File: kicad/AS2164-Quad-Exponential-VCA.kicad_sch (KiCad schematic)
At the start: 71 parts, among them J1 CV1, J10 CV4, J11 Audio_in_4, J12 Audio_out_4, J2 Audio_in_1, J3 Audio_out_1, J4 CV2, J5 Audio_in_2, J6 Audio_out_2, J7 CV3, J8 Audio_in_3, J9 Audio_out_3, U1 TL074, U2 AS2164, U3 TL074

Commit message: added Schematic Revision 0.1.1
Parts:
- R11, R18, R25, R4: value 30K -> 100K
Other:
- note added: "VCA Inputs Vc1, Vc2, Vc3, Vc4 3.3V = 100% attenuation 0V = unity gain Vc < 0V = +20dB gain"
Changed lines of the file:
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@@
     (title "Eurorack AS2164 Quad Exponential VCA")
     (date "2024-01-25")
-    (rev "0.1.0")
+    (rev "0.1.1")
     (company "DIYSynthMNL")
     (comment 1 "This version is a prototype")
@@
     (effects (font (size 3 3)) (justify left bottom))
   )
+  (text "10Vpp" (at 270.51 45.72 0)
+    (effects (font (size 1.27 1.27)) (justify left bottom))
+  )
   (text "10Vpp" (at 177.8 115.57 0)
     (effects (font (size 1.27 1.27)) (justify left bottom))
@@
     (effects (font (size 2 2)) (justify left bottom))
   )
+  (text "10Vpp" (at 124.46 106.68 0)
+    (effects (font (size 1.27 1.27)) (justify left bottom))
+  )
   (text "0-5V" (at 13.97 91.44 0)
     (effects (font (size 1.27 1.27)) (justify left bottom))
@@
     (effects (font (size 1.27 1.27)) (justify left bottom))
   )
+  (text "10Vpp" (at 270.51 106.68 0)
+    (effects (font (size 1.27 1.27)) (justify left bottom))
+  )
   (text "0-5V" (at 158.75 30.48 0)
     (effects (font (size 1.27 1.27)) (justify left bottom))
@@
     (effects (font (size 2 2)) (justify left bottom))
   )
+  (text "10Vpp" (at 125.73 45.72 0)
+    (effects (font (size 1.27 1.27)) (justify left bottom))
+  )
   (text "0-5V" (at 158.75 91.44 0)
     (effects (font (size 1.27 1.27)) (justify left bottom))
@@
     (effects (font (size 2 2)) (justify left bottom))
   )
+  (text "VCA Inputs Vc1, Vc2, Vc3, Vc4\n3.3V = 100% attenuation\n0V = unity gain\nVc < 0V = +20dB gain"
+    (at 83.82 24.13 0)
+    (effects (font (size 1.27 1.27)) (justify left bottom))
+  )
   (text "10Vpp" (at 177.8 54.61 0)
     (effects (font (size 1.27 1.27)) (justify left bottom))
@@
       (effects (font (size 1.27 1.27)))
     )
-    (property "Value" "30K" (at 102.87 107.95 90)
+    (property "Value" "100K" (at 102.87 107.95 90)
       (effects (font (size 1.27 1.27)))
     )
@@
       (effects (font (size 1.27 1.27)))
     )
-    (property "Value" "30K" (at 247.65 46.99 90)
+    (property "Value" "100K" (at 247.65 46.99 90)
       (effects (font (size 1.27 1.27)))
     )
@@
       (effects (font (size 1.27 1.27)))
     )
-    (property "Value" "30K" (at 247.65 107.95 90)
+    (property "Value" "100K" (at 247.65 107.95 90)
       (effects (font (size 1.27 1.27)))
     )
@@
       (effects (font (size 1.27 1.27)))
     )
-    (property "Value" "30K" (at 102.87 46.99 90)
+    (property "Value" "100K" (at 102.87 46.99 90)
       (effects (font (size 1.27 1.27)))
     )

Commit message: schematic rev 0.1.1 notes added
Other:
- note added: "Module CV inputs (jacks) 0V CV = 100% attenuation 5V CV = Unity Gain"
- note removed: "0V CV = 100% attenuation 5V CV = Unity Gain"
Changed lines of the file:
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@@
     (effects (font (size 1.27 1.27)) (justify left bottom))
   )
-  (text "0V CV = 100% attenuation\n5V CV = Unity Gain" (at 180.34 143.51 0)
+  (text "Module CV inputs (jacks)\n0V CV = 100% attenuation\n5V CV = Unity Gain"
+    (at 180.34 148.59 0)
     (effects (font (size 1.27 1.27)) (justify left bottom))
   )
@@
   )
   (text "VCA Inputs Vc1, Vc2, Vc3, Vc4\n3.3V = 100% attenuation\n0V = unity gain\nVc < 0V = +20dB gain"
-    (at 83.82 24.13 0)
+    (at 180.34 158.75 0)
     (effects (font (size 1.27 1.27)) (justify left bottom))
   )

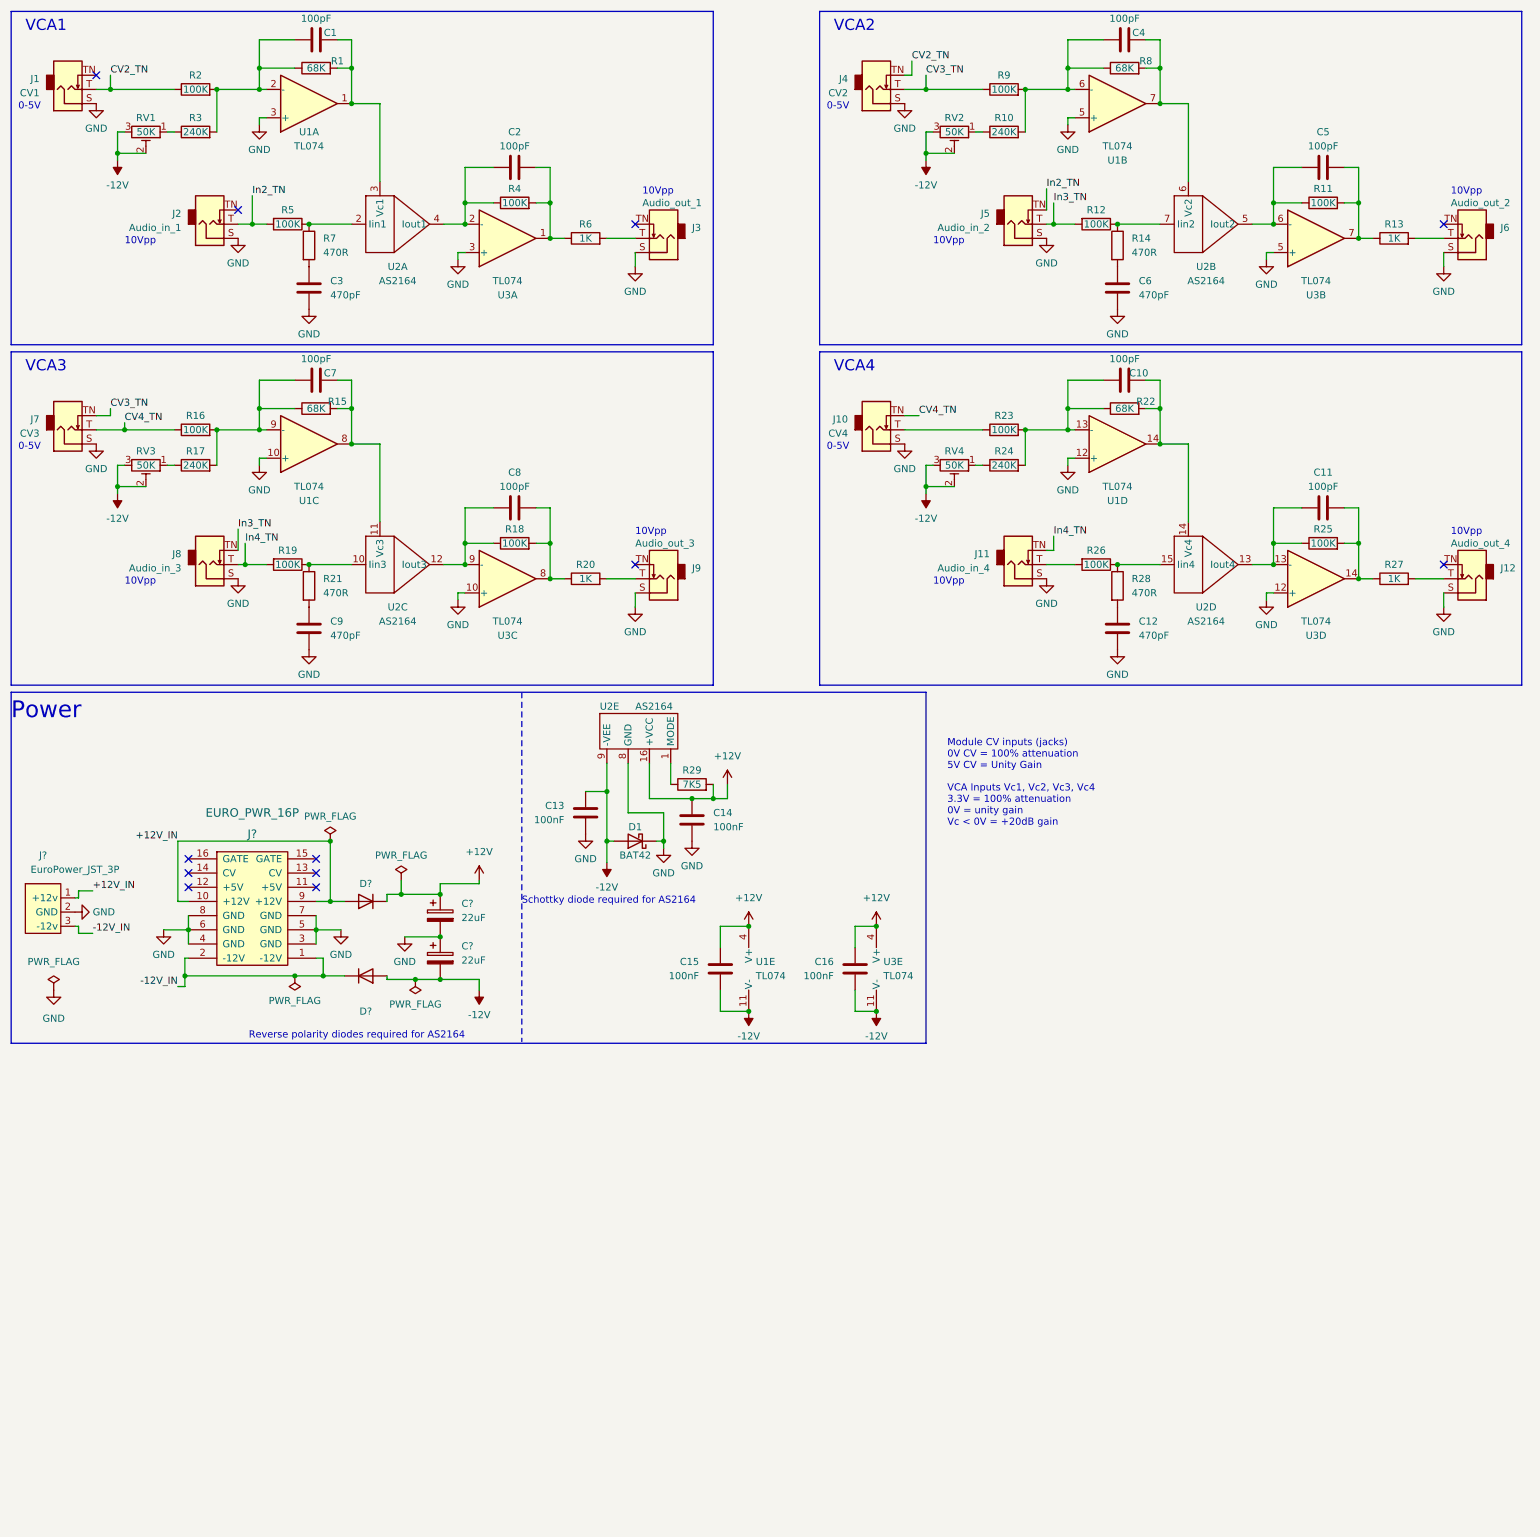
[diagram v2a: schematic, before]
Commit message: Added schematic rev 0.1.2
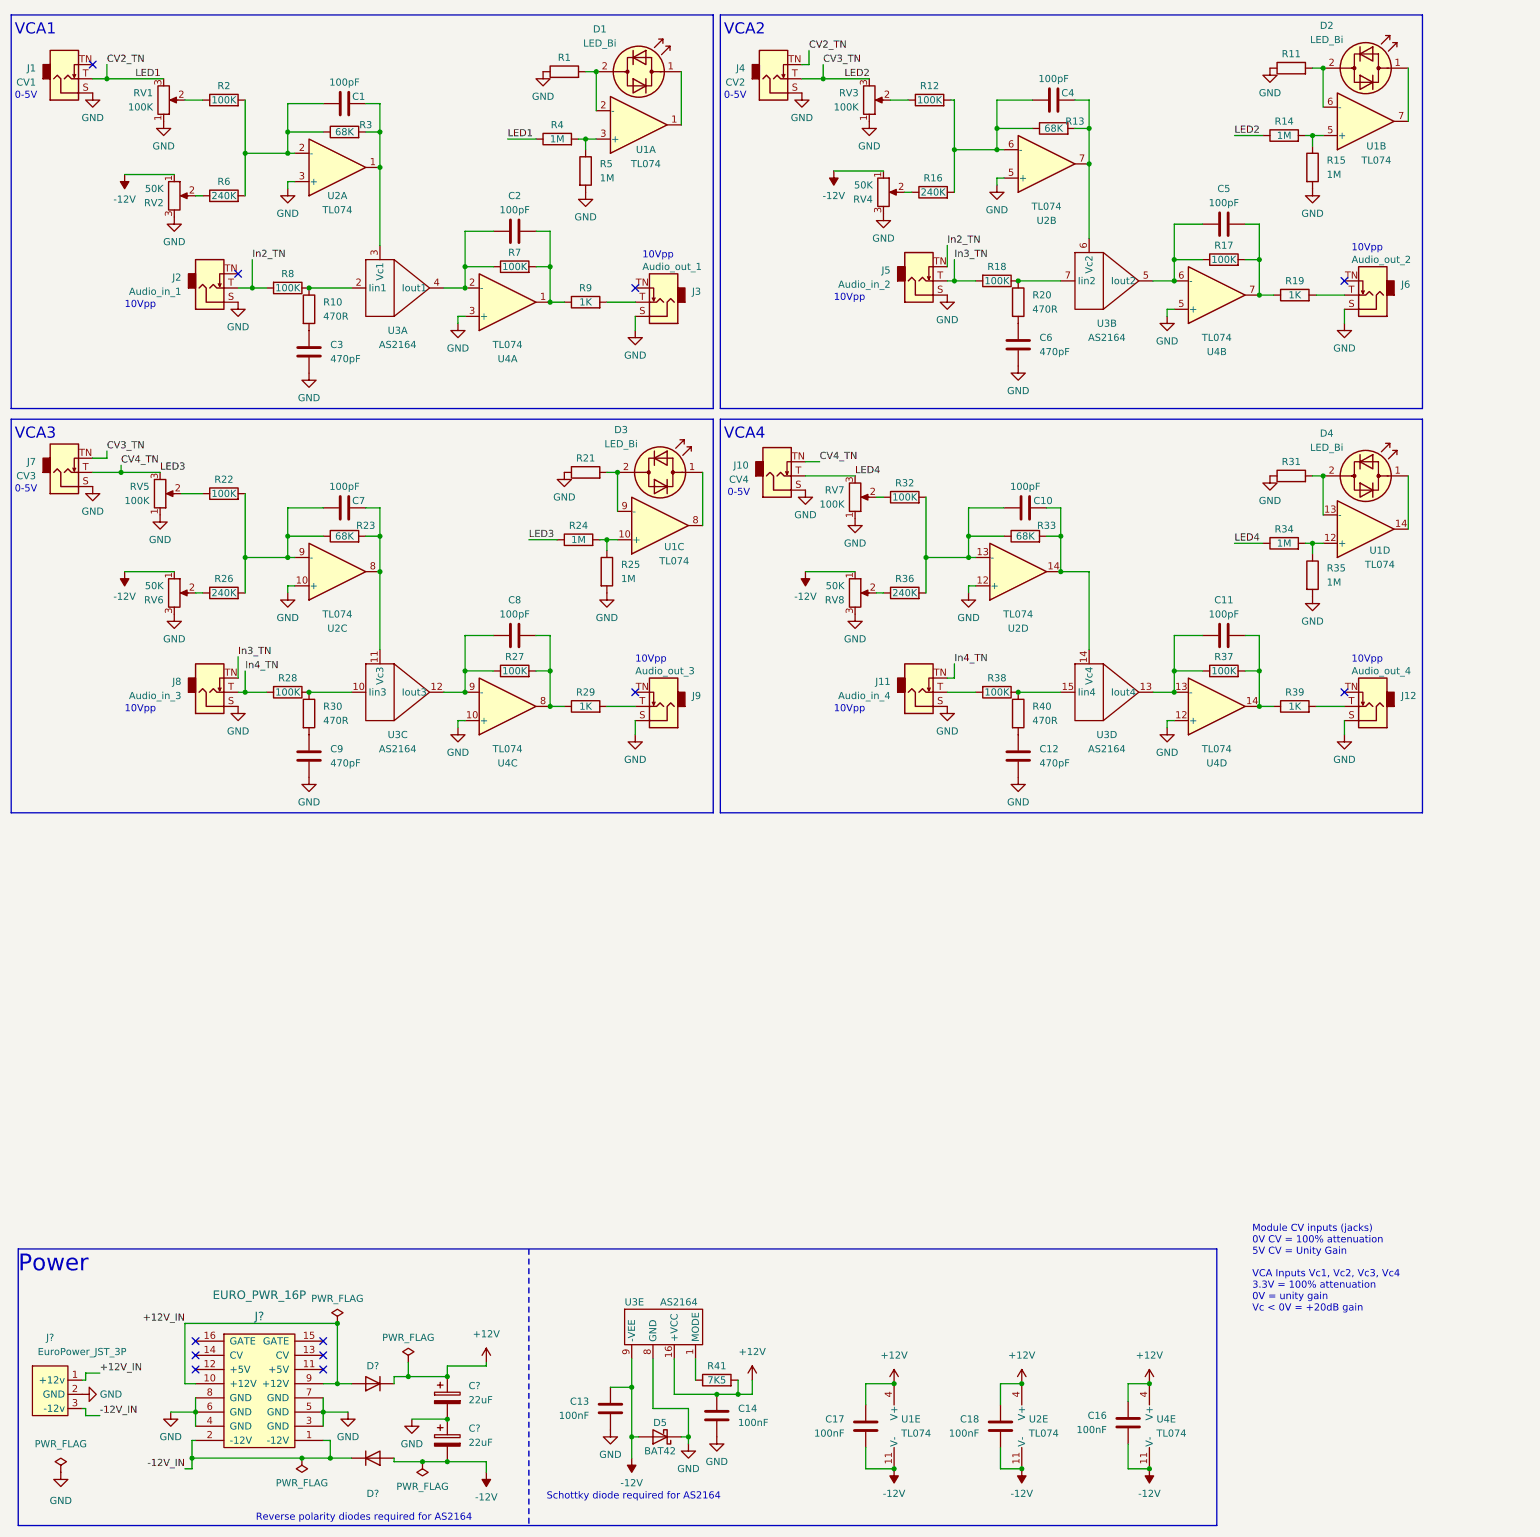
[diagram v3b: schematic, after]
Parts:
- removed RV1, RV2, RV3, RV4: 50K, symbol Device:R_Potentiometer_Trim
- added C16: 100nF, symbol Device:C
- added D1, D2, D3, D4: LED_Bi, symbol Device:LED_Dual_Bidirectional
- added R1, R11, R21, R31: ~, symbol Device:R
- added R14, R15, R24, R25, R34, R35, R4, R5: 1M, symbol Device:R
- added RV1, RV3, RV5, RV7: 100K, symbol Device:R_Potentiometer
- added RV2, RV4, RV6, RV8: 50K, symbol Device:R_Potentiometer
- added unit 4 of U1
- added unit 3 of U1
- added unit 2 of U1
- added unit 1 of U1
- added unit 5 of U4
- renumbered C15 to C17, C16 to C18, D1 to D5, R7 to R10, R9 to R12, R8 to R13, R10 to R16, R11 to R17, R12 to R18, R13 to R19, R14 to R20, R16 to R22, R15 to R23, R17 to R26, R18 to R27, R19 to R28, R20 to R29, R1 to R3, R21 to R30, R23 to R32, R22 to R33, R24 to R36, R25 to R37, R26 to R38, R27 to R39, R28 to R40, R29 to R41, R3 to R6, R4 to R7, R5 to R8, R6 to R9, U1 to U2, U3 to U2, U2 to U3, U3 to U4
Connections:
- net +12V: now also C16.1, U4.4 (V+)
- net -12V: now also C16.2, RV2.1, RV4.1, RV6.1, RV8.1, U4.11 (V-)
- net CV2_TN: now also R4.1, RV1.3; no longer R2.1
- net CV3_TN: now also R14.1, RV3.3; no longer R12.1
- net CV4_TN: now also R24.1, RV5.3; no longer R22.1
- net GND: now also R1.1, R11.1, R15.2, R21.1, R25.2, R31.1, R35.2, R5.2, RV1.1, RV2.3, RV3.1, RV4.3, RV5.1, RV6.3, RV7.1, RV8.3
- net at R36.1: now also RV8.2
- net at R16.1: now also RV4.2
- net at R32.1: now also RV7.2; no longer J10.T
- net at R26.1: now also RV6.2
- net at R6.1: now also RV2.2
- new net: R34.2, R35.1, U1.12 (+)
- new net: D4.2 (AK), R31.2, U1.13 (-)
- new net: D4.1 (KA), U1.14
- new net: R24.2, R25.1, U1.10 (+)
- new net: D3.1 (KA), U1.8
- new net: D3.2 (AK), R21.2, U1.9 (-)
- new net: R14.2, R15.1, U1.5 (+)
- new net: R12.1, RV3.2
- new net: D2.1 (KA), U1.7
- new net: D2.2 (AK), R11.2, U1.6 (-)
- new net: D1.1 (KA), U1.1
- new net: D1.2 (AK), R1.2, U1.2 (-)
- new net: R2.1, RV1.2
- new net: R4.2, R5.1, U1.3 (+)
- new net: R22.1, RV5.2
- new net LED4: J10.T, R34.1, RV7.3
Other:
- moved on the sheet: C1, C10, C11, C12, C13, C14, C17, C18, C2, C3, C4, C5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

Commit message: added schem rev0.1.3
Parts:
- added C20: 100nF, symbol Device:C
- added C21, C22: 100pF, symbol Device:C
- added JP1: Mix/VCA4, symbol Jumper:Jumper_3_Bridged12
- added R42, R43, R44, R45, R46, R47, R48: 100K, symbol Device:R
- added U5: TL072, symbol Amplifier_Operational:TL072
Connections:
- net +12V: now also C20.1, U5.8 (V+)
- net -12V: now also C20.2, U5.4 (V-)
- net GND: now also U5.3 (+), U5.5 (+)
- net O1: now reaches C2.2, R7.2, R9.1, U4.1
- net O1: now also R43.1
- net O2: now reaches C5.2, R17.2, R19.1, U4.7
- net O2: now also R44.1
- net O3: now reaches C8.2, R27.2, R29.1, U4.8
- net O3: now also R45.1
- net O4: now reaches C11.2, R37.2, U4.14
- net O4: now also JP1.3 (B), R46.1; no longer R39.1
- new net: C22.1, R47.2, R48.1, U5.6 (-)
- new net: C21.2, R42.2, R47.1, U5.1
- new net: C21.1, R42.1, R43.2, R44.2, R45.2, R46.2, U5.2 (-)
- new net: JP1.2 (C), R39.1
- new net Mix Out: C22.2, JP1.1 (A), R48.2, U5.7
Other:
- note added: "Audio Out 4 select"
- note added: "Mix"
- moved on the sheet: J12, R39

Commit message: Add revision 0.1.4
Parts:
- added D10, D11, D12, D13, D14, D15, D8, D9: BAT42, symbol Device:D_Schottky
- R47, R48: value 100K -> 10K
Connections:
- net at U2.7, U3.6 (Vc2): now also D10.2 (A), D11.1 (K); no longer C4.2, R13.2
- net at C10.1, R32.2, R33.1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: now also D15.2 (A)
- net at C10.2, R33.2: now also D14.1 (K); no longer U2.14, U3.14 (Vc4)
- net at U2.1, U3.3 (Vc1): now also D8.1 (K), D9.2 (A); no longer C1.2, R3.2
- net at C4.1, R12.2, R13.1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: now also D11.2 (A)
- net at C1.1, R2.2, R3.1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: now also D8.2 (A)
- net at C7.1, R22.2, R23.1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: now also D13.2 (A)
- net at C7.2, R23.2: now also D12.1 (K); no longer U2.8, U3.11 (Vc3)
- new net: D14.2 (A), D15.1 (K), U2.14, U3.14 (Vc4)
- new net: C4.2, D10.1 (K), R13.2
- new net: C1.2, D9.1 (K), R3.2
- new net: D12.2 (A), D13.1 (K), U2.8, U3.11 (Vc3)
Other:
- note added: "Added vca cv input protection diodes to input stage opamps. Changed mixed output op amp resistors to 10k. Rev 0.1.4."
- moved on the sheet: C1, C10, C4, C7, R13, R23, R3, R33
